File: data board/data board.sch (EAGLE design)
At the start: 41 parts, among them IC1 93LC56B, IC2 FT232HQ, U1 CJT1117-5.0-SOT223, X3 HUSB238, X6 USBC, Y1 12MHz

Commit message: v1.1
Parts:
- U1: LCSC (none) -> C89273
- renumbered U$9 to U9
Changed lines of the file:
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@@
 <part name="U$3" library="microbuilder" deviceset="GND" device=""/>
 <part name="JP3" library="microbuilder" deviceset="HEADER-1X3" device="ROUND"/>
-<part name="U1" library="Seeed-IC" library_urn="urn:adsk.eagle:library:470" deviceset="PMIC-CJT1117-5.0(SOT223)" device="" package3d_urn="urn:adsk.eagle:package:32638/1" value="CJT1117-5.0-SOT223"/>
+<part name="U1" library="Seeed-IC" library_urn="urn:adsk.eagle:library:470" deviceset="PMIC-CJT1117-5.0(SOT223)" device="" package3d_urn="urn:adsk.eagle:package:32638/1" value="CJT1117-5.0-SOT223">
+<attribute name="LCSC" value="C89273"/>
+</part>
 <part name="U$8" library="microbuilder" deviceset="GND" device=""/>
-<part name="U$9" library="SparkFun-DiscreteSemi" deviceset="MOSFET-PCHANNEL-SOIC8" device="SOIC8">
+<part name="U9" library="SparkFun-DiscreteSemi" deviceset="MOSFET-PCHANNEL-SOIC8" device="SOIC8">
 <attribute name="LCSC" value="C143671"/>
 </part>
@@
 <attribute name="NAME" x="307.34" y="135.89" size="1.27" layer="95"/>
 <attribute name="VALUE" x="314.96" y="135.89" size="1.27" layer="96"/>
+<attribute name="LCSC" x="314.96" y="132.08" size="1.778" layer="96" display="off"/>
 </instance>
 <instance part="U$8" gate="G$1" x="314.96" y="121.92" smashed="yes">
 <attribute name="VALUE" x="313.436" y="119.38" size="1.27" layer="96"/>
 </instance>
-<instance part="U$9" gate="G$1" x="248.92" y="124.46" smashed="yes">
+<instance part="U9" gate="G$1" x="248.92" y="124.46" smashed="yes">
 <attribute name="NAME" x="241.3" y="130.048" size="1.778" layer="95"/>
 <attribute name="VALUE" x="241.3" y="114.3" size="1.778" layer="96"/>
@@
 </segment>
 <segment>
-<pinref part="U$9" gate="G$1" pin="S@1"/>
+<pinref part="U9" gate="G$1" pin="S@1"/>
 <wire x1="238.76" y1="127" x2="226.06" y2="127" width="0.1524" layer="91"/>
-<pinref part="U$9" gate="G$1" pin="S@2"/>
+<pinref part="U9" gate="G$1" pin="S@2"/>
 <wire x1="238.76" y1="127" x2="238.76" y2="124.46" width="0.1524" layer="91"/>
 <junction x="238.76" y="127"/>
-<pinref part="U$9" gate="G$1" pin="S@3"/>
+<pinref part="U9" gate="G$1" pin="S@3"/>
 <wire x1="238.76" y1="124.46" x2="238.76" y2="121.92" width="0.1524" layer="91"/>
 <junction x="238.76" y="124.46"/>
@@
 </segment>
 <segment>
-<pinref part="U$9" gate="G$1" pin="D@4"/>
-<pinref part="U$9" gate="G$1" pin="D@3"/>
+<pinref part="U9" gate="G$1" pin="D@4"/>
+<pinref part="U9" gate="G$1" pin="D@3"/>
 <wire x1="256.54" y1="127" x2="256.54" y2="124.46" width="0.1524" layer="91"/>
-<pinref part="U$9" gate="G$1" pin="D@2"/>
+<pinref part="U9" gate="G$1" pin="D@2"/>
 <wire x1="256.54" y1="124.46" x2="256.54" y2="121.92" width="0.1524" layer="91"/>
 <junction x="256.54" y="124.46"/>
-<pinref part="U$9" gate="G$1" pin="D@1"/>
+<pinref part="U9" gate="G$1" pin="D@1"/>
 <wire x1="256.54" y1="121.92" x2="256.54" y2="119.38" width="0.1524" layer="91"/>
 <junction x="256.54" y="121.92"/>
@@
 </segment>
 <segment>
-<pinref part="U$9" gate="G$1" pin="G"/>
+<pinref part="U9" gate="G$1" pin="G"/>
 <wire x1="238.76" y1="119.38" x2="226.06" y2="119.38" width="0.1524" layer="91"/>
 <label x="226.06" y="119.38" size="1.778" layer="95"/>

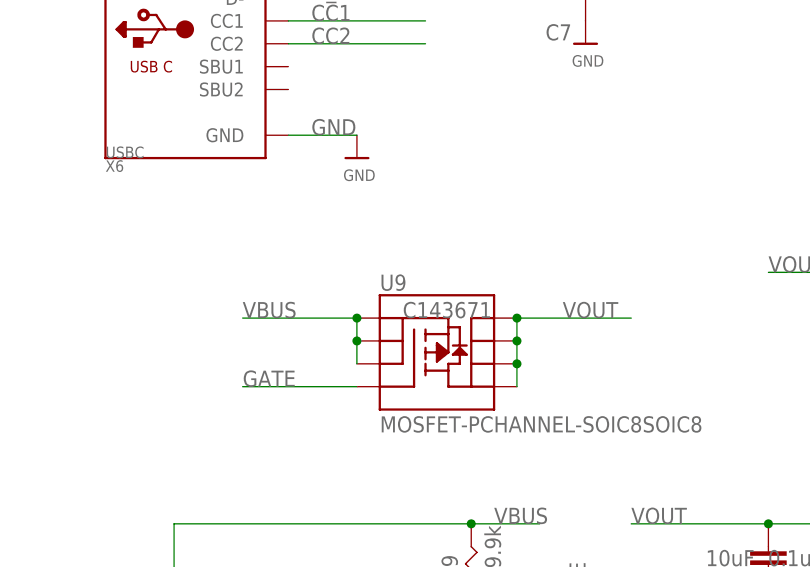
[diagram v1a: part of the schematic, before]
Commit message: Revert "v1.1"
This reverts commit 9c2a8abd0e838ea48c804dee952ae91d8fcae4a4.
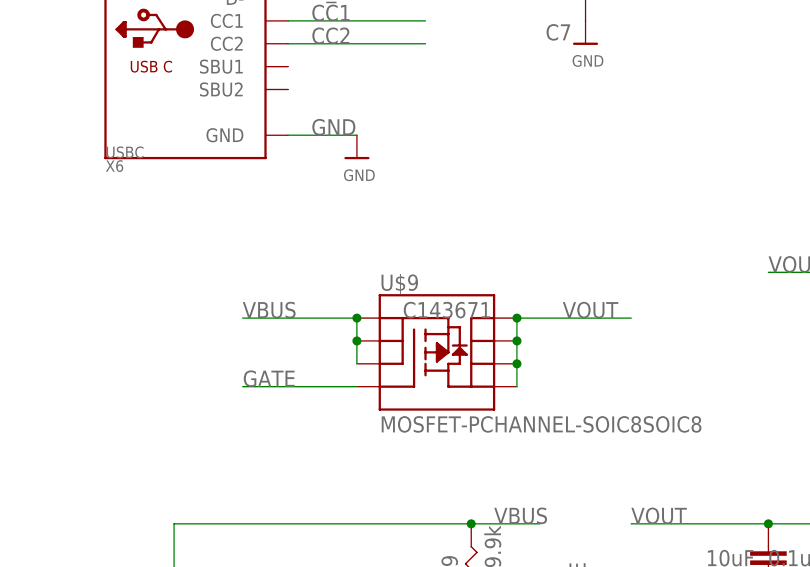
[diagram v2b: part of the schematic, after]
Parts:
- U1: LCSC C89273 -> (none)
- renumbered U9 to U$9
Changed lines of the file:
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@@
 <part name="U$3" library="microbuilder" deviceset="GND" device=""/>
 <part name="JP3" library="microbuilder" deviceset="HEADER-1X3" device="ROUND"/>
-<part name="U1" library="Seeed-IC" library_urn="urn:adsk.eagle:library:470" deviceset="PMIC-CJT1117-5.0(SOT223)" device="" package3d_urn="urn:adsk.eagle:package:32638/1" value="CJT1117-5.0-SOT223">
-<attribute name="LCSC" value="C89273"/>
-</part>
+<part name="U1" library="Seeed-IC" library_urn="urn:adsk.eagle:library:470" deviceset="PMIC-CJT1117-5.0(SOT223)" device="" package3d_urn="urn:adsk.eagle:package:32638/1" value="CJT1117-5.0-SOT223"/>
 <part name="U$8" library="microbuilder" deviceset="GND" device=""/>
-<part name="U9" library="SparkFun-DiscreteSemi" deviceset="MOSFET-PCHANNEL-SOIC8" device="SOIC8">
+<part name="U$9" library="SparkFun-DiscreteSemi" deviceset="MOSFET-PCHANNEL-SOIC8" device="SOIC8">
 <attribute name="LCSC" value="C143671"/>
 </part>
@@
 <attribute name="NAME" x="307.34" y="135.89" size="1.27" layer="95"/>
 <attribute name="VALUE" x="314.96" y="135.89" size="1.27" layer="96"/>
-<attribute name="LCSC" x="314.96" y="132.08" size="1.778" layer="96" display="off"/>
 </instance>
 <instance part="U$8" gate="G$1" x="314.96" y="121.92" smashed="yes">
 <attribute name="VALUE" x="313.436" y="119.38" size="1.27" layer="96"/>
 </instance>
-<instance part="U9" gate="G$1" x="248.92" y="124.46" smashed="yes">
+<instance part="U$9" gate="G$1" x="248.92" y="124.46" smashed="yes">
 <attribute name="NAME" x="241.3" y="130.048" size="1.778" layer="95"/>
 <attribute name="VALUE" x="241.3" y="114.3" size="1.778" layer="96"/>
@@
 </segment>
 <segment>
-<pinref part="U9" gate="G$1" pin="S@1"/>
+<pinref part="U$9" gate="G$1" pin="S@1"/>
 <wire x1="238.76" y1="127" x2="226.06" y2="127" width="0.1524" layer="91"/>
-<pinref part="U9" gate="G$1" pin="S@2"/>
+<pinref part="U$9" gate="G$1" pin="S@2"/>
 <wire x1="238.76" y1="127" x2="238.76" y2="124.46" width="0.1524" layer="91"/>
 <junction x="238.76" y="127"/>
-<pinref part="U9" gate="G$1" pin="S@3"/>
+<pinref part="U$9" gate="G$1" pin="S@3"/>
 <wire x1="238.76" y1="124.46" x2="238.76" y2="121.92" width="0.1524" layer="91"/>
 <junction x="238.76" y="124.46"/>
@@
 </segment>
 <segment>
-<pinref part="U9" gate="G$1" pin="D@4"/>
-<pinref part="U9" gate="G$1" pin="D@3"/>
+<pinref part="U$9" gate="G$1" pin="D@4"/>
+<pinref part="U$9" gate="G$1" pin="D@3"/>
 <wire x1="256.54" y1="127" x2="256.54" y2="124.46" width="0.1524" layer="91"/>
-<pinref part="U9" gate="G$1" pin="D@2"/>
+<pinref part="U$9" gate="G$1" pin="D@2"/>
 <wire x1="256.54" y1="124.46" x2="256.54" y2="121.92" width="0.1524" layer="91"/>
 <junction x="256.54" y="124.46"/>
-<pinref part="U9" gate="G$1" pin="D@1"/>
+<pinref part="U$9" gate="G$1" pin="D@1"/>
 <wire x1="256.54" y1="121.92" x2="256.54" y2="119.38" width="0.1524" layer="91"/>
 <junction x="256.54" y="121.92"/>
@@
 </segment>
 <segment>
-<pinref part="U9" gate="G$1" pin="G"/>
+<pinref part="U$9" gate="G$1" pin="G"/>
 <wire x1="238.76" y1="119.38" x2="226.06" y2="119.38" width="0.1524" layer="91"/>
 <label x="226.06" y="119.38" size="1.778" layer="95"/>

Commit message: Revert "v1.1"
This reverts commit 3ea246ff6ce0038198bb0009f8cc6fa5045fb056.
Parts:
- added R3, R5: 5.1k, FlashPCB_Resistors:RES-0402
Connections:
- removed net 5VD: C19.2, C20.2, FB1.1, U1.OUT
- net 5V: now also C19.2, C20.2, U1.OUT
- net CC1: now also R5.P$2
- net CC2: now also R3.P$2
- net GND: now also R3.P$1, R5.P$1
- net VBUS: now also FB1.1
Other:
- moved on the sheet: C13, C7, FB1, X6

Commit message: v1.1
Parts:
- removed R3, R5: 5.1k, FlashPCB_Resistors:RES-0402
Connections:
- new net 5VD: C19.2, C20.2, FB1.1, U1.OUT
- net 5V: no longer C19.2, C20.2, U1.OUT
- net CC1: no longer R5.P$2
- net CC2: no longer R3.P$2
- net GND: no longer R3.P$1, R5.P$1
- net VBUS: no longer FB1.1
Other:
- moved on the sheet: C13, C7, FB1, X6
